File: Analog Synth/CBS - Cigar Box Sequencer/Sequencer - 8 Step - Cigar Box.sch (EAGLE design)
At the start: 205 parts, among them IC1 TL084P, IC10 79L05, IC11 MCP6002, IC12 74AC138N, IC13 74ALS04N, IC14 74AC138N, IC15 74ALS04N, IC16 74ALS04N, IC17 74ALS08N, IC2 TL084P, IC3 TL084P, IC4 74ALS04N, IC5 4050N, IC6 78L05, IC7 40193N, IC8 78L05, IC9 74LS86N, Q1 I/O, Q14 J310, Q15 J310, Q16 J310, Q17 J310, Q18 J310, Q19 J310, Q2 I/O, Q20 J310, Q3 I/O, Q4 2N3906, Q5 2N3904, Q6 J310, X1 I/O, X2 I/O, X3 I/O

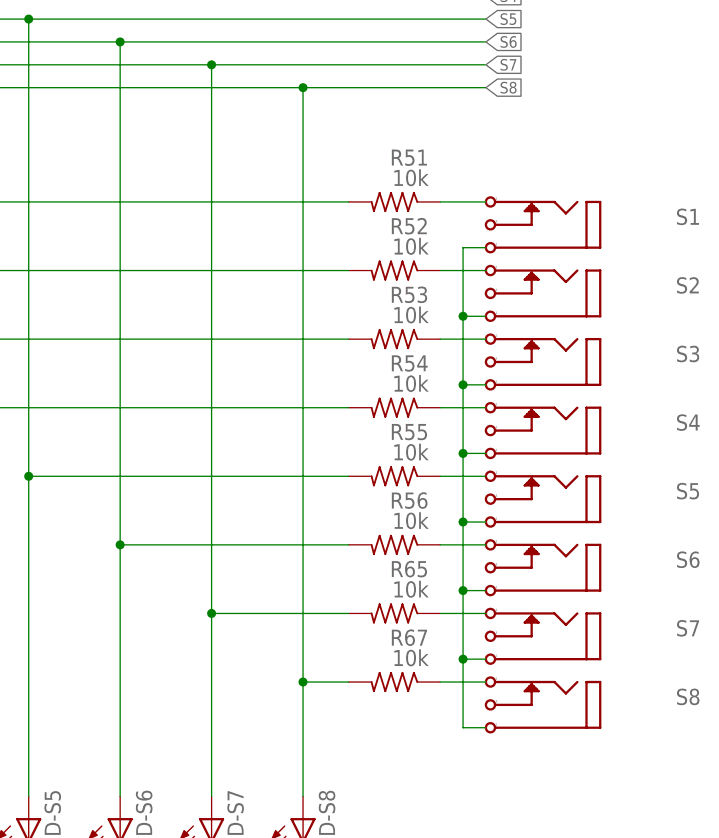
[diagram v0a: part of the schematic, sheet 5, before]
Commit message: CBS: fixed output resistor values
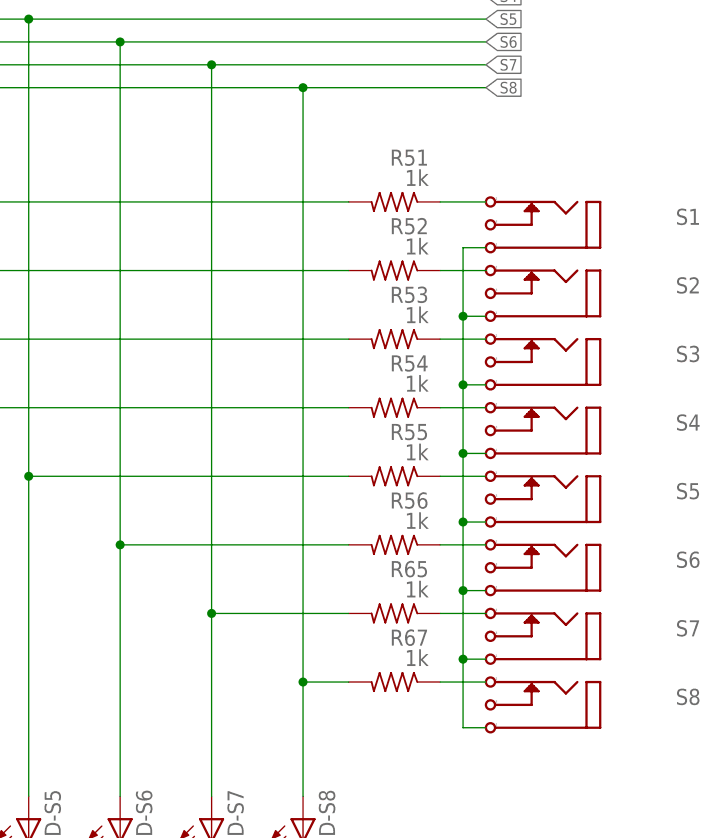
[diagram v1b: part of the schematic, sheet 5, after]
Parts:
- R51, R52, R53, R54, R55, R56, R65, R67: value 10k -> 1k
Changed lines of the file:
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@@
 <part name="S7" library="!synth_sch" deviceset="MONO_JACK" device="" value="I/O"/>
 <part name="S8" library="!synth_sch" deviceset="MONO_JACK" device="" value="I/O"/>
-<part name="R51" library="rcl" deviceset="R-US_" device="R0603" value="10k"/>
-<part name="R52" library="rcl" deviceset="R-US_" device="R0603" value="10k"/>
-<part name="R53" library="rcl" deviceset="R-US_" device="R0603" value="10k"/>
-<part name="R54" library="rcl" deviceset="R-US_" device="R0603" value="10k"/>
-<part name="R55" library="rcl" deviceset="R-US_" device="R0603" value="10k"/>
-<part name="R56" library="rcl" deviceset="R-US_" device="R0603" value="10k"/>
-<part name="R65" library="rcl" deviceset="R-US_" device="R0603" value="10k"/>
-<part name="R67" library="rcl" deviceset="R-US_" device="R0603" value="10k"/>
+<part name="R51" library="rcl" deviceset="R-US_" device="R0603" value="1k"/>
+<part name="R52" library="rcl" deviceset="R-US_" device="R0603" value="1k"/>
+<part name="R53" library="rcl" deviceset="R-US_" device="R0603" value="1k"/>
+<part name="R54" library="rcl" deviceset="R-US_" device="R0603" value="1k"/>
+<part name="R55" library="rcl" deviceset="R-US_" device="R0603" value="1k"/>
+<part name="R56" library="rcl" deviceset="R-US_" device="R0603" value="1k"/>
+<part name="R65" library="rcl" deviceset="R-US_" device="R0603" value="1k"/>
+<part name="R67" library="rcl" deviceset="R-US_" device="R0603" value="1k"/>
 <part name="GATE_OUT" library="!synth_sch" deviceset="MONO_JACK" device="" value="I/O"/>
 <part name="LED_GATE_OUT" library="led" deviceset="TLLG4400" device="" value=""/>

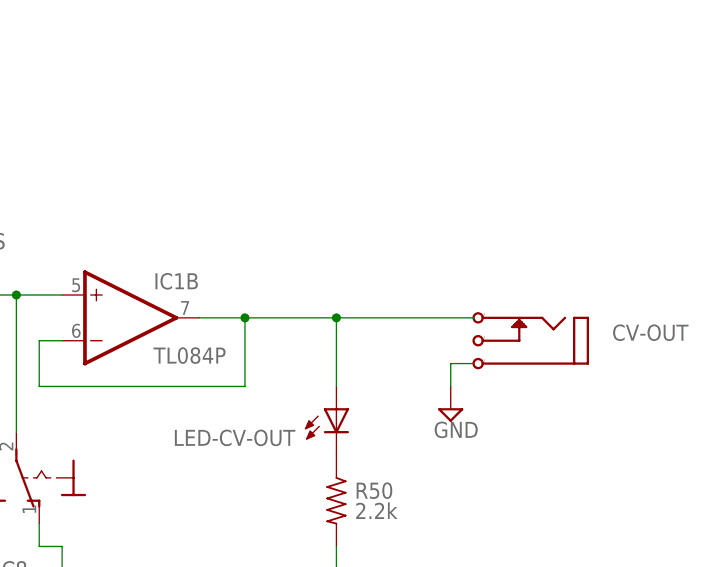
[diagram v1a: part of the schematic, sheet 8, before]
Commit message: CBS: fixed output resistor values - other ones
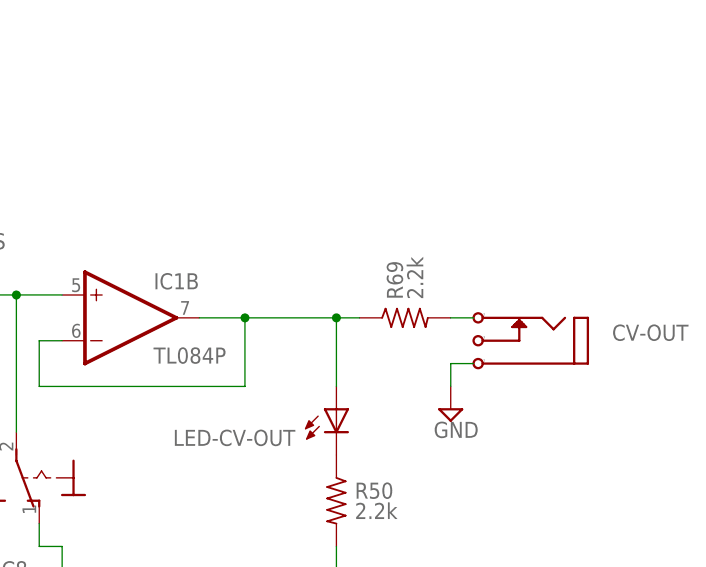
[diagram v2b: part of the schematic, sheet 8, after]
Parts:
- added R69: 2.2k, rcl:R-US_R0603
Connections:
- new net N$124: CV-OUT.P2, R69.2
- net N$108: now also R69.1; no longer CV-OUT.P2
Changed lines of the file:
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@@
 <part name="SUPPLY50" library="supply2" deviceset="GND" device=""/>
 <part name="IC17" library="74xx-us" deviceset="74*08" device="N" technology="ALS"/>
+<part name="R69" library="rcl" deviceset="R-US_" device="R0603" value="2.2k"/>
 </parts>
 <sheets>
@@
 <instance part="SUPPLY39" gate="-5V" x="35.56" y="-5.08"/>
 <instance part="SUPPLY40" gate="GND" x="83.82" y="27.94"/>
+<instance part="R69" gate="G$1" x="78.74" y="38.1" smashed="yes">
+<attribute name="NAME" x="78.5114" y="40.132" size="1.778" layer="95" rot="R90"/>
+<attribute name="VALUE" x="80.772" y="40.132" size="1.778" layer="96" rot="R90"/>
+</instance>
 </instances>
 <busses>
@@
 <wire x1="71.12" y1="38.1" x2="71.12" y2="30.48" width="0.1524" layer="91"/>
 <junction x="60.96" y="38.1"/>
+<pinref part="R69" gate="G$1" pin="1"/>
+<wire x1="73.66" y1="38.1" x2="71.12" y2="38.1" width="0.1524" layer="91"/>
 <junction x="71.12" y="38.1"/>
-<pinref part="CV-OUT" gate="J1" pin="P2"/>
-<wire x1="71.12" y1="38.1" x2="86.36" y2="38.1" width="0.1524" layer="91"/>
 </segment>
 </net>
@@
 </segment>
 </net>
+<net name="N$124" class="0">
+<segment>
+<pinref part="R69" gate="G$1" pin="2"/>
+<pinref part="CV-OUT" gate="J1" pin="P2"/>
+<wire x1="83.82" y1="38.1" x2="86.36" y2="38.1" width="0.1524" layer="91"/>
+</segment>
+</net>

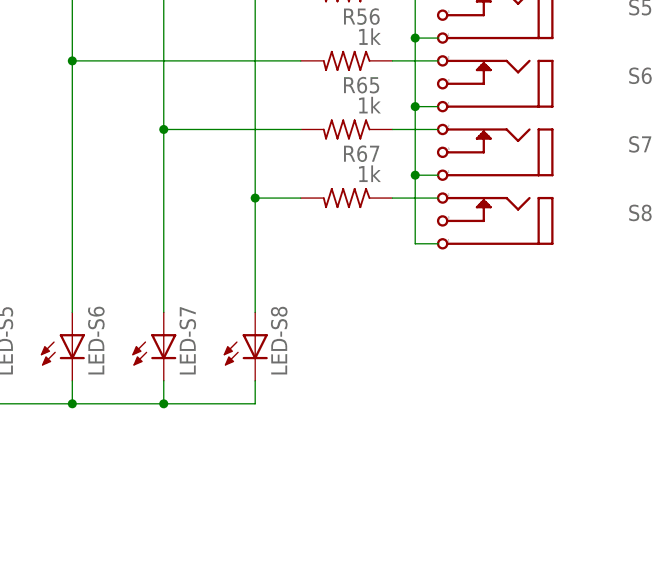
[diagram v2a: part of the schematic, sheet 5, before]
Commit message: CBS: fixed output jack ground issue
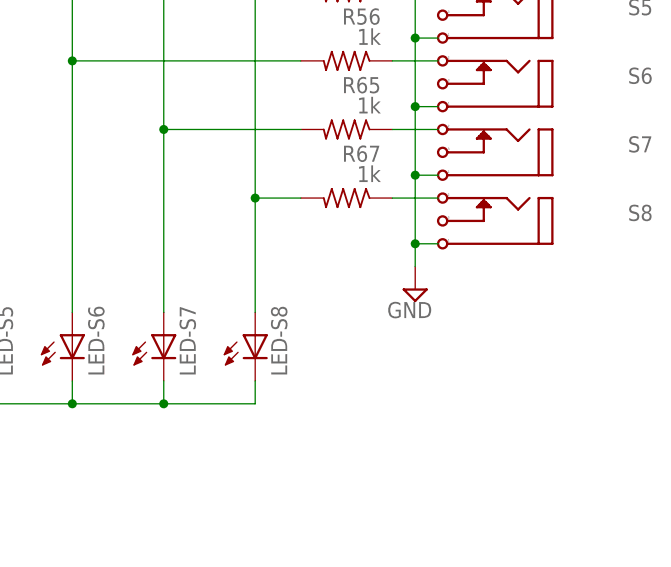
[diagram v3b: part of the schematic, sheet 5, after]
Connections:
- removed net N$123: S1.P$1, S2.P$1, S3.P$1, S4.P$1, S5.P$1, S6.P$1, S7.P$1, S8.P$1
- net GND: now also S1.P$1, S2.P$1, S3.P$1, S4.P$1, S5.P$1, S6.P$1, S7.P$1, S8.P$1
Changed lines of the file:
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@@
 <part name="IC17" library="74xx-us" deviceset="74*08" device="N" technology="ALS"/>
 <part name="R69" library="rcl" deviceset="R-US_" device="R0603" value="2.2k"/>
+<part name="SUPPLY51" library="supply2" deviceset="GND" device=""/>
 </parts>
 <sheets>
@@
 <instance part="IC16" gate="E" x="-27.94" y="-22.86"/>
 <instance part="IC16" gate="F" x="-27.94" y="-35.56"/>
+<instance part="SUPPLY51" gate="GND" x="162.56" y="-10.16" rot="MR0"/>
 </instances>
 <busses>
@@
 <pinref part="R37" gate="G$1" pin="1"/>
 <pinref part="SUPPLY32" gate="GND" pin="GND"/>
+</segment>
+<segment>
+<pinref part="S1" gate="J1" pin="P$1"/>
+<wire x1="165.1" y1="48.26" x2="162.56" y2="48.26" width="0.1524" layer="91"/>
+<wire x1="162.56" y1="48.26" x2="162.56" y2="40.64" width="0.1524" layer="91"/>
+<pinref part="S2" gate="J1" pin="P$1"/>
+<wire x1="165.1" y1="40.64" x2="162.56" y2="40.64" width="0.1524" layer="91"/>
+<wire x1="162.56" y1="40.64" x2="162.56" y2="33.02" width="0.1524" layer="91"/>
+<pinref part="S3" gate="J1" pin="P$1"/>
+<wire x1="165.1" y1="33.02" x2="162.56" y2="33.02" width="0.1524" layer="91"/>
+<wire x1="162.56" y1="33.02" x2="162.56" y2="25.4" width="0.1524" layer="91"/>
+<pinref part="S4" gate="J1" pin="P$1"/>
+<wire x1="165.1" y1="25.4" x2="162.56" y2="25.4" width="0.1524" layer="91"/>
+<wire x1="162.56" y1="25.4" x2="162.56" y2="17.78" width="0.1524" layer="91"/>
+<pinref part="S5" gate="J1" pin="P$1"/>
+<wire x1="165.1" y1="17.78" x2="162.56" y2="17.78" width="0.1524" layer="91"/>
+<wire x1="162.56" y1="17.78" x2="162.56" y2="10.16" width="0.1524" layer="91"/>
+<pinref part="S6" gate="J1" pin="P$1"/>
+<wire x1="165.1" y1="10.16" x2="162.56" y2="10.16" width="0.1524" layer="91"/>
+<wire x1="162.56" y1="10.16" x2="162.56" y2="2.54" width="0.1524" layer="91"/>
+<pinref part="S7" gate="J1" pin="P$1"/>
+<wire x1="165.1" y1="2.54" x2="162.56" y2="2.54" width="0.1524" layer="91"/>
+<wire x1="162.56" y1="2.54" x2="162.56" y2="-5.08" width="0.1524" layer="91"/>
+<pinref part="S8" gate="J1" pin="P$1"/>
+<wire x1="162.56" y1="-5.08" x2="165.1" y2="-5.08" width="0.1524" layer="91"/>
+<junction x="162.56" y="2.54"/>
+<junction x="162.56" y="10.16"/>
+<junction x="162.56" y="17.78"/>
+<junction x="162.56" y="25.4"/>
+<junction x="162.56" y="33.02"/>
+<junction x="162.56" y="40.64"/>
+<junction x="162.56" y="-5.08"/>
+<wire x1="162.56" y1="-5.08" x2="162.56" y2="-7.62" width="0.1524" layer="91"/>
+<pinref part="SUPPLY51" gate="GND" pin="GND"/>
 </segment>
 </net>
@@
 </segment>
 </net>
-<net name="N$123" class="0">
-<segment>
-<pinref part="S1" gate="J1" pin="P$1"/>
-<wire x1="165.1" y1="48.26" x2="162.56" y2="48.26" width="0.1524" layer="91"/>
-<wire x1="162.56" y1="48.26" x2="162.56" y2="40.64" width="0.1524" layer="91"/>
-<pinref part="S2" gate="J1" pin="P$1"/>
-<wire x1="165.1" y1="40.64" x2="162.56" y2="40.64" width="0.1524" layer="91"/>
-<wire x1="162.56" y1="40.64" x2="162.56" y2="33.02" width="0.1524" layer="91"/>
-<pinref part="S3" gate="J1" pin="P$1"/>
-<wire x1="165.1" y1="33.02" x2="162.56" y2="33.02" width="0.1524" layer="91"/>
-<wire x1="162.56" y1="33.02" x2="162.56" y2="25.4" width="0.1524" layer="91"/>
-<pinref part="S4" gate="J1" pin="P$1"/>
-<wire x1="165.1" y1="25.4" x2="162.56" y2="25.4" width="0.1524" layer="91"/>
-<wire x1="162.56" y1="25.4" x2="162.56" y2="17.78" width="0.1524" layer="91"/>
-<pinref part="S5" gate="J1" pin="P$1"/>
-<wire x1="165.1" y1="17.78" x2="162.56" y2="17.78" width="0.1524" layer="91"/>
-<wire x1="162.56" y1="17.78" x2="162.56" y2="10.16" width="0.1524" layer="91"/>
-<pinref part="S6" gate="J1" pin="P$1"/>
-<wire x1="165.1" y1="10.16" x2="162.56" y2="10.16" width="0.1524" layer="91"/>
-<wire x1="162.56" y1="10.16" x2="162.56" y2="2.54" width="0.1524" layer="91"/>
-<pinref part="S7" gate="J1" pin="P$1"/>
-<wire x1="165.1" y1="2.54" x2="162.56" y2="2.54" width="0.1524" layer="91"/>
-<wire x1="162.56" y1="2.54" x2="162.56" y2="-5.08" width="0.1524" layer="91"/>
-<pinref part="S8" gate="J1" pin="P$1"/>
-<wire x1="162.56" y1="-5.08" x2="165.1" y2="-5.08" width="0.1524" layer="91"/>
-<junction x="162.56" y="2.54"/>
-<junction x="162.56" y="10.16"/>
-<junction x="162.56" y="17.78"/>
-<junction x="162.56" y="25.4"/>
-<junction x="162.56" y="33.02"/>
-<junction x="162.56" y="40.64"/>
-</segment>
-</net>

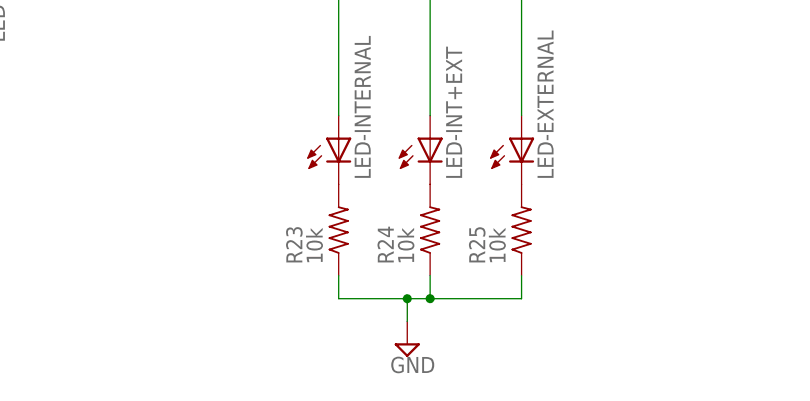
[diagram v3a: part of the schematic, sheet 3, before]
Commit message: CBS: removed unnecessary resistors
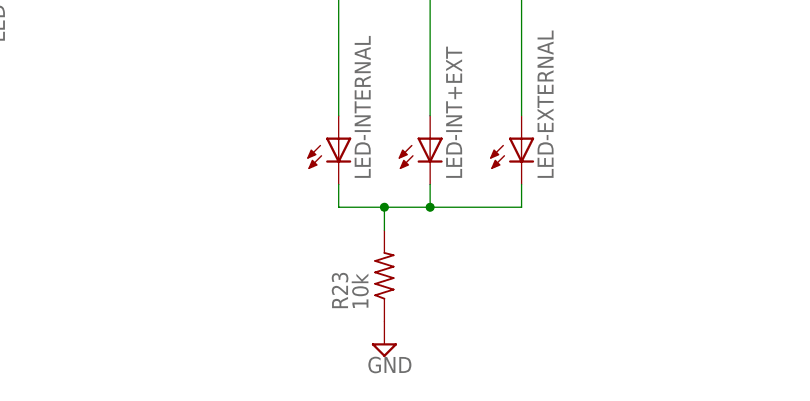
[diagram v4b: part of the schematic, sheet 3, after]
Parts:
- removed R24, R25: 10k, rcl:R-US_R0603
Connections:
- removed net N$52: LED-INT+EXT.C, R24.2
- removed net N$53: LED-EXTERNAL.C, R25.2
- net GND: no longer R24.1, R25.1
- net N$51: now also LED-EXTERNAL.C, LED-INT+EXT.C
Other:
- moved on the sheet: R23
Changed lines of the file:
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@@
 <part name="IC9" library="74xx-us" deviceset="74*86" device="N" technology="LS"/>
 <part name="R23" library="rcl" deviceset="R-US_" device="R0603" value="10k"/>
-<part name="R24" library="rcl" deviceset="R-US_" device="R0603" value="10k"/>
-<part name="R25" library="rcl" deviceset="R-US_" device="R0603" value="10k"/>
 <part name="SUPPLY15" library="supply2" deviceset="GND" device=""/>
 <part name="R36" library="rcl" deviceset="R-US_" device="R0603" value="2.2k"/>
@@
 <instance part="SUPPLY13" gate="GND" x="91.44" y="58.42"/>
 <instance part="IC9" gate="A" x="83.82" y="38.1"/>
-<instance part="R23" gate="G$1" x="109.22" y="-10.16" smashed="yes" rot="R90">
-<attribute name="NAME" x="105.1814" y="-13.97" size="1.778" layer="95" rot="R90"/>
-<attribute name="VALUE" x="107.442" y="-13.97" size="1.778" layer="96" rot="R90"/>
-</instance>
-<instance part="R24" gate="G$1" x="119.38" y="-10.16" smashed="yes" rot="R90">
-<attribute name="NAME" x="115.3414" y="-13.97" size="1.778" layer="95" rot="R90"/>
-<attribute name="VALUE" x="117.602" y="-13.97" size="1.778" layer="96" rot="R90"/>
-</instance>
-<instance part="R25" gate="G$1" x="129.54" y="-10.16" smashed="yes" rot="R90">
-<attribute name="NAME" x="125.5014" y="-13.97" size="1.778" layer="95" rot="R90"/>
-<attribute name="VALUE" x="127.762" y="-13.97" size="1.778" layer="96" rot="R90"/>
-</instance>
-<instance part="SUPPLY15" gate="GND" x="116.84" y="-22.86"/>
+<instance part="R23" gate="G$1" x="114.3" y="-15.24" smashed="yes" rot="R90">
+<attribute name="NAME" x="110.2614" y="-19.05" size="1.778" layer="95" rot="R90"/>
+<attribute name="VALUE" x="112.522" y="-19.05" size="1.778" layer="96" rot="R90"/>
+</instance>
+<instance part="SUPPLY15" gate="GND" x="114.3" y="-22.86"/>
 <instance part="R36" gate="G$1" x="5.08" y="81.28" smashed="yes" rot="R270">
 <attribute name="NAME" x="9.1186" y="85.09" size="1.778" layer="95" rot="R270"/>
@@
 <wire x1="88.9" y1="63.5" x2="91.44" y2="63.5" width="0.1524" layer="91"/>
 <wire x1="91.44" y1="63.5" x2="91.44" y2="60.96" width="0.1524" layer="91"/>
-</segment>
-<segment>
-<pinref part="R23" gate="G$1" pin="1"/>
-<wire x1="109.22" y1="-15.24" x2="109.22" y2="-17.78" width="0.1524" layer="91"/>
-<pinref part="R25" gate="G$1" pin="1"/>
-<wire x1="109.22" y1="-17.78" x2="116.84" y2="-17.78" width="0.1524" layer="91"/>
-<wire x1="116.84" y1="-17.78" x2="119.38" y2="-17.78" width="0.1524" layer="91"/>
-<wire x1="129.54" y1="-15.24" x2="129.54" y2="-17.78" width="0.1524" layer="91"/>
-<wire x1="129.54" y1="-17.78" x2="119.38" y2="-17.78" width="0.1524" layer="91"/>
-<pinref part="R24" gate="G$1" pin="1"/>
-<wire x1="119.38" y1="-17.78" x2="119.38" y2="-15.24" width="0.1524" layer="91"/>
-<junction x="119.38" y="-17.78"/>
-<pinref part="SUPPLY15" gate="GND" pin="GND"/>
-<wire x1="116.84" y1="-20.32" x2="116.84" y2="-17.78" width="0.1524" layer="91"/>
-<junction x="116.84" y="-17.78"/>
 </segment>
 <segment>
@@
 <wire x1="35.56" y1="15.24" x2="35.56" y2="12.7" width="0.1524" layer="91"/>
 <pinref part="SUPPLY27" gate="GND" pin="GND"/>
+</segment>
+<segment>
+<pinref part="R23" gate="G$1" pin="1"/>
+<pinref part="SUPPLY15" gate="GND" pin="GND"/>
 </segment>
 </net>
@@
 <segment>
 <pinref part="LED-INTERNAL" gate="G$1" pin="C"/>
+<wire x1="109.22" y1="-7.62" x2="109.22" y2="-5.08" width="0.1524" layer="91"/>
+<wire x1="109.22" y1="-7.62" x2="114.3" y2="-7.62" width="0.1524" layer="91"/>
+<pinref part="LED-INT+EXT" gate="G$1" pin="C"/>
+<wire x1="114.3" y1="-7.62" x2="119.38" y2="-7.62" width="0.1524" layer="91"/>
+<wire x1="119.38" y1="-5.08" x2="119.38" y2="-7.62" width="0.1524" layer="91"/>
+<wire x1="119.38" y1="-7.62" x2="129.54" y2="-7.62" width="0.1524" layer="91"/>
+<pinref part="LED-EXTERNAL" gate="G$1" pin="C"/>
+<wire x1="129.54" y1="-7.62" x2="129.54" y2="-5.08" width="0.1524" layer="91"/>
+<junction x="119.38" y="-7.62"/>
 <pinref part="R23" gate="G$1" pin="2"/>
-</segment>
-</net>
-<net name="N$52" class="0">
-<segment>
-<pinref part="LED-INT+EXT" gate="G$1" pin="C"/>
-<pinref part="R24" gate="G$1" pin="2"/>
-</segment>
-</net>
-<net name="N$53" class="0">
-<segment>
-<pinref part="LED-EXTERNAL" gate="G$1" pin="C"/>
-<pinref part="R25" gate="G$1" pin="2"/>
-</segment>
-</net>
+<wire x1="114.3" y1="-10.16" x2="114.3" y2="-7.62" width="0.1524" layer="91"/>
+<junction x="114.3" y="-7.62"/>
+</segment>
+</net>

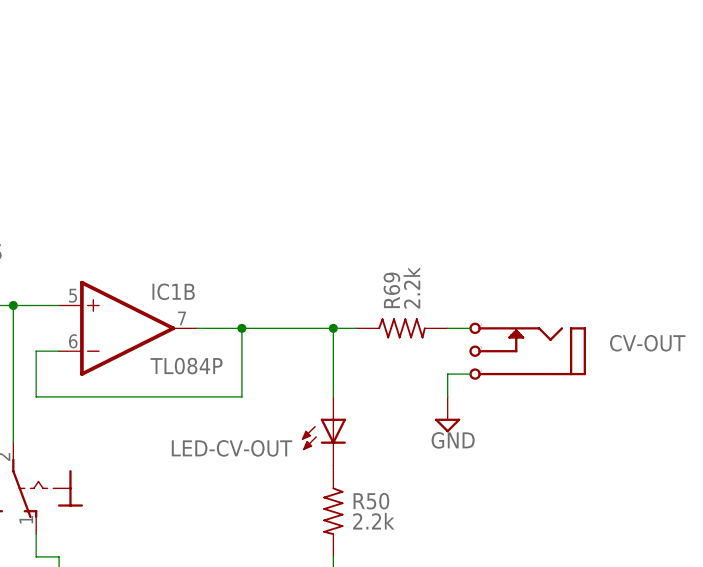
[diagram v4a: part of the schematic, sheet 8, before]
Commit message: CBS: fixed the CV-OUT resistor value from 2.2k to 1k
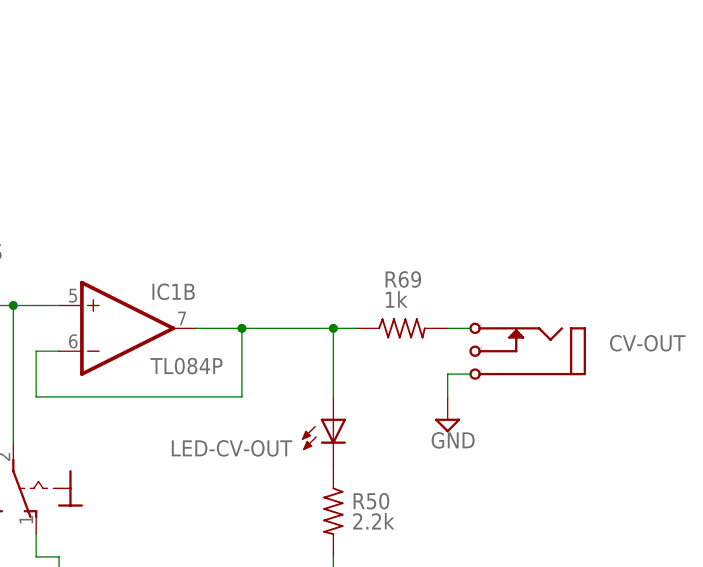
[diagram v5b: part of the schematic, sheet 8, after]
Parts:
- R69: value 2.2k -> 1k
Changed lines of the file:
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@@
 <part name="SUPPLY50" library="supply2" deviceset="GND" device=""/>
 <part name="IC17" library="74xx-us" deviceset="74*08" device="N" technology="ALS"/>
-<part name="R69" library="rcl" deviceset="R-US_" device="R0603" value="2.2k"/>
+<part name="R69" library="rcl" deviceset="R-US_" device="R0603" value="1k"/>
 <part name="SUPPLY51" library="supply2" deviceset="GND" device=""/>
 </parts>
@@
 <instance part="SUPPLY40" gate="GND" x="83.82" y="27.94"/>
 <instance part="R69" gate="G$1" x="78.74" y="38.1" smashed="yes">
-<attribute name="NAME" x="78.5114" y="40.132" size="1.778" layer="95" rot="R90"/>
-<attribute name="VALUE" x="80.772" y="40.132" size="1.778" layer="96" rot="R90"/>
+<attribute name="NAME" x="76.708" y="42.6466" size="1.778" layer="95"/>
+<attribute name="VALUE" x="76.708" y="40.386" size="1.778" layer="96"/>
 </instance>
 </instances>
